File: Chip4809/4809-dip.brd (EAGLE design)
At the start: 58.7 x 20.3 mm, 20 parts

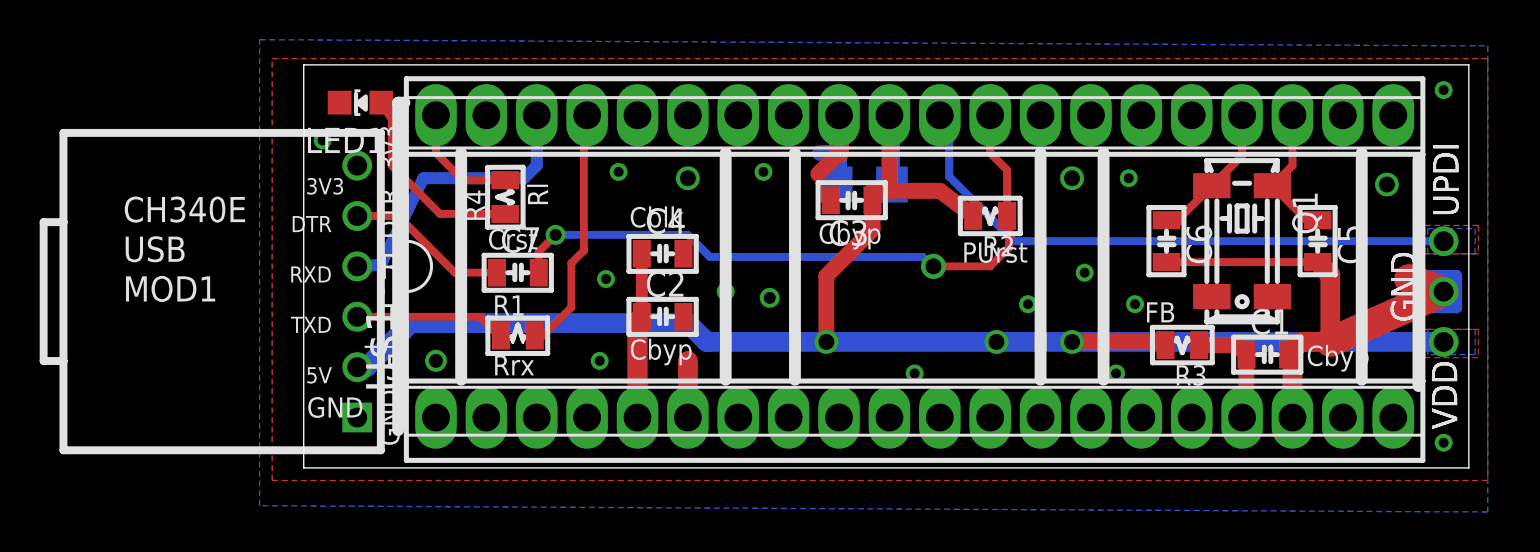
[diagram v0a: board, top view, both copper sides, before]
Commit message: Version 0.4 fix RX/TX, move UPDI pin
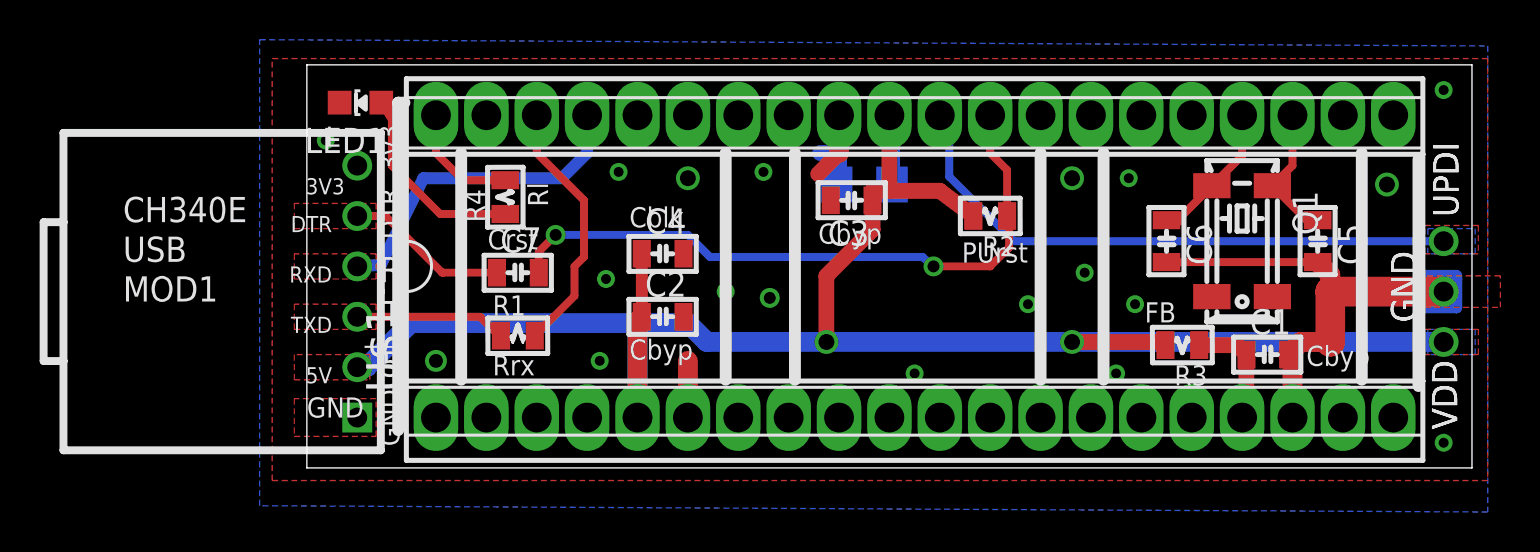
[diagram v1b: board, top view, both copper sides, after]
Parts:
- VS1: value 0.2 -> 0.3
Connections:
- net CPURX: now also U$1.38; no longer U$1.37
- net CPUTX: now also U$1.37; no longer U$1.38
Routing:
- net CPUTX: track 14.6 -> 16.7 mm
- net CPURX: track 12.5 -> 13.1 mm
- net VCC: vias 3 -> 2
- added copper zone on layer 1, net CPUTX
- added copper zone on layer 1, net N$8
- added copper zone on layer 1, net USBTX
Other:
- board text added: "20190830 by WestfW: RX/TX reversed, damn it. Fix."
- board text added: "L"
